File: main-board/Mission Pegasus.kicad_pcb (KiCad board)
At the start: 2 copper layers, 90.2 x 95.9 mm, 35 parts, among them J1 TC2030, M1 MountingHole, M2 MountingHole, M3 MountingHole, M4 MountingHole, Q1 DTC113Z, U2 4MB Flash, U3 AS72652, U4 AS72653, U6 AS72651, U7 RASPBERRY_PI_ZERO_2_W

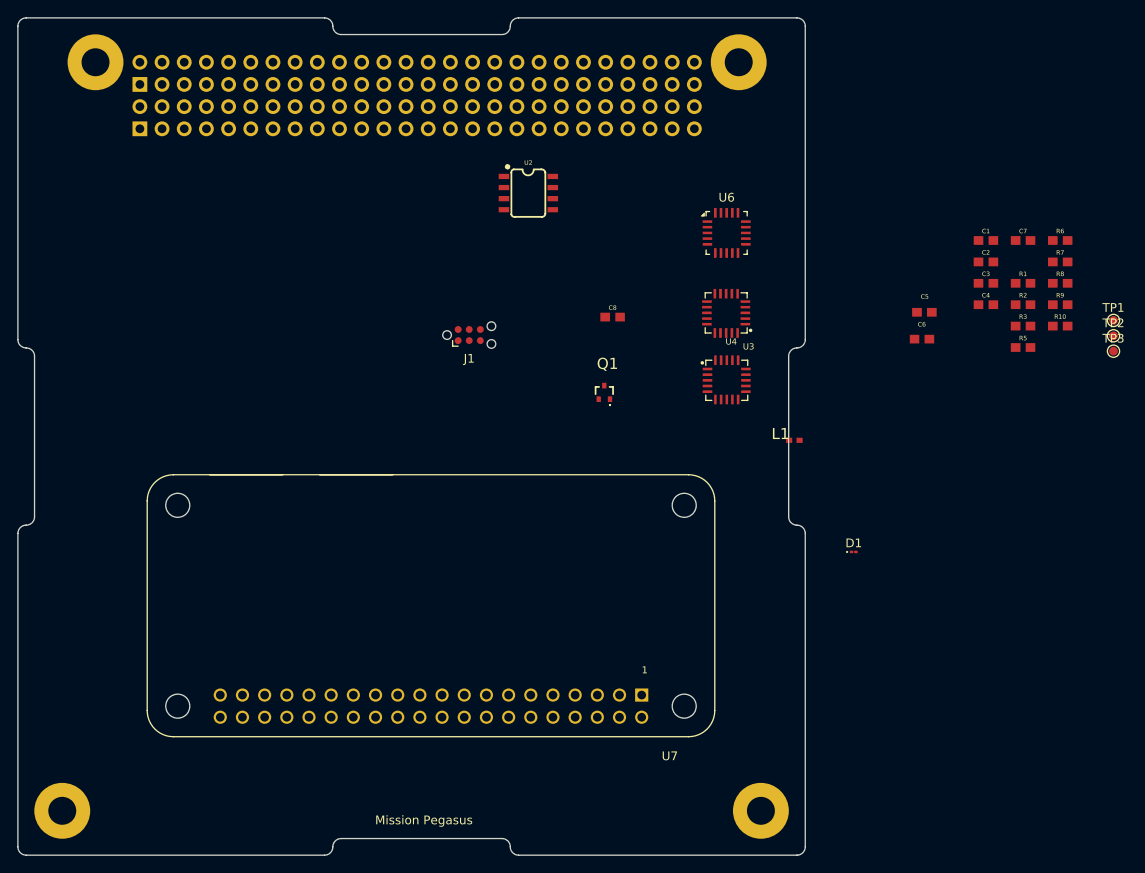
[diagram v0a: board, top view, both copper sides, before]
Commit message: Add Amphenol 20021311-00020T4LF (Minitek127) to mezzanine libraries
Import the Library Loader part (20-pin 1.27mm board-to-board connector)
into the mezzanine's SamacSys_Parts library: footprint, 3D model, and
symbol appended. 3D path rewritten to ${KIPRJMOD}-relative and the
symbol's Footprint property qualified with the library nickname.
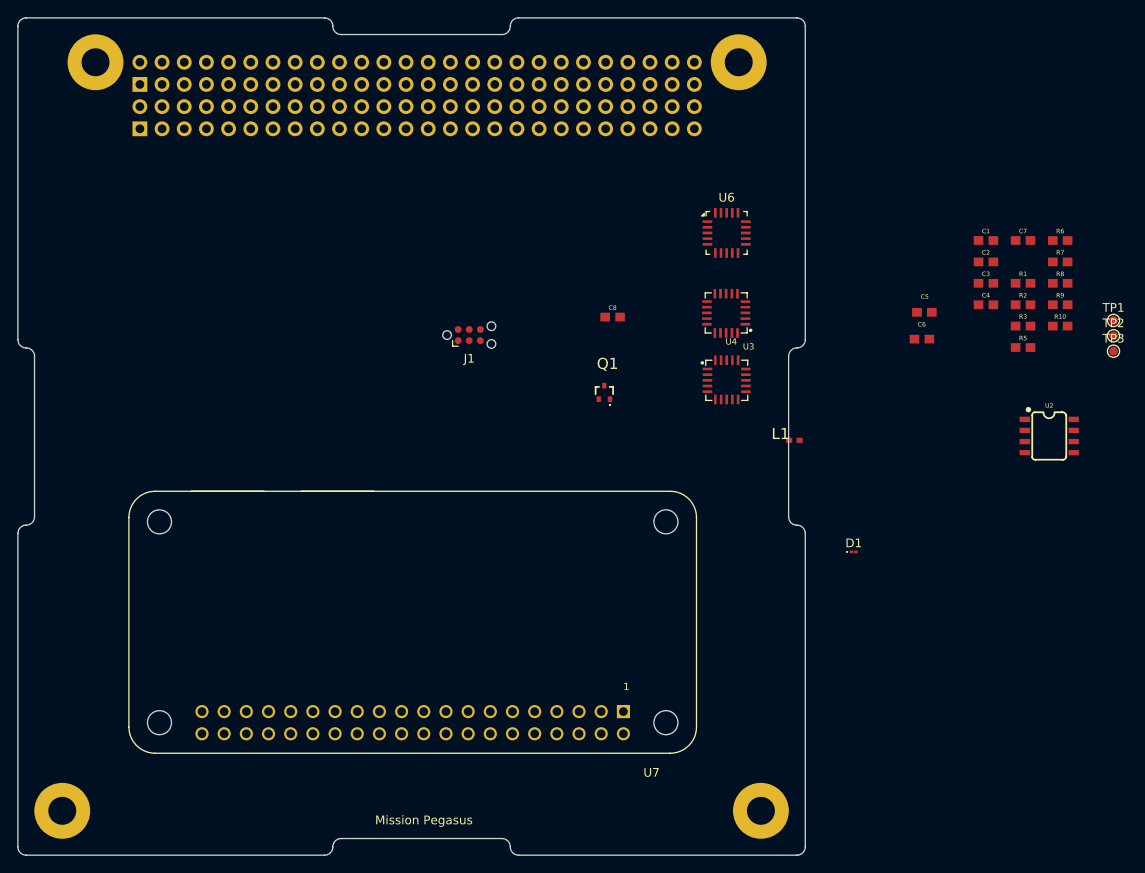
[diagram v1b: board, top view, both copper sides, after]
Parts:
- moved U2 65.8 mm to (209.1, 93.5)
- moved U7 2.82 mm to (136.2, 126.3)
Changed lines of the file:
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@@
 	(footprint "RPIZERO:RASPBERRYPI-ZERO_RPI-ZERO"
 		(layer "F.Cu")
-		(at 138.3075 124.4337 180)
+		(at 136.212 126.326 180)
 		(descr "Raspberry Pi board model B+, full outline with position of big connectors &amp; drill holes")
 		(property "Reference" "U7"
@@
 	(footprint "SparkfunLibrary:4MbFlash"
 		(layer "F.Cu")
-		(at 149.4581 65.681 -90)
+		(at 209.11 93.494 -90)
 		(descr "SOIC, 0.15 inch width")
 		(property "Reference" "U2"

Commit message: Attach Raspberry Pi Zero 2 W 3D model to RPi footprint
Add the mechanical STEP model of the Raspberry Pi Zero 2 W board
(RaspberryPi_Zero_2W.step, from the downloaded SolidWorks CAD) to
main-board 3dmodels, and reference it from the RASPBERRYPI-ZERO_RPI-ZERO
footprint via a ${KIPRJMOD}-relative path. Offset/rotation set to zero as
a starting point - needs alignment tuning in KiCad's 3D tab.
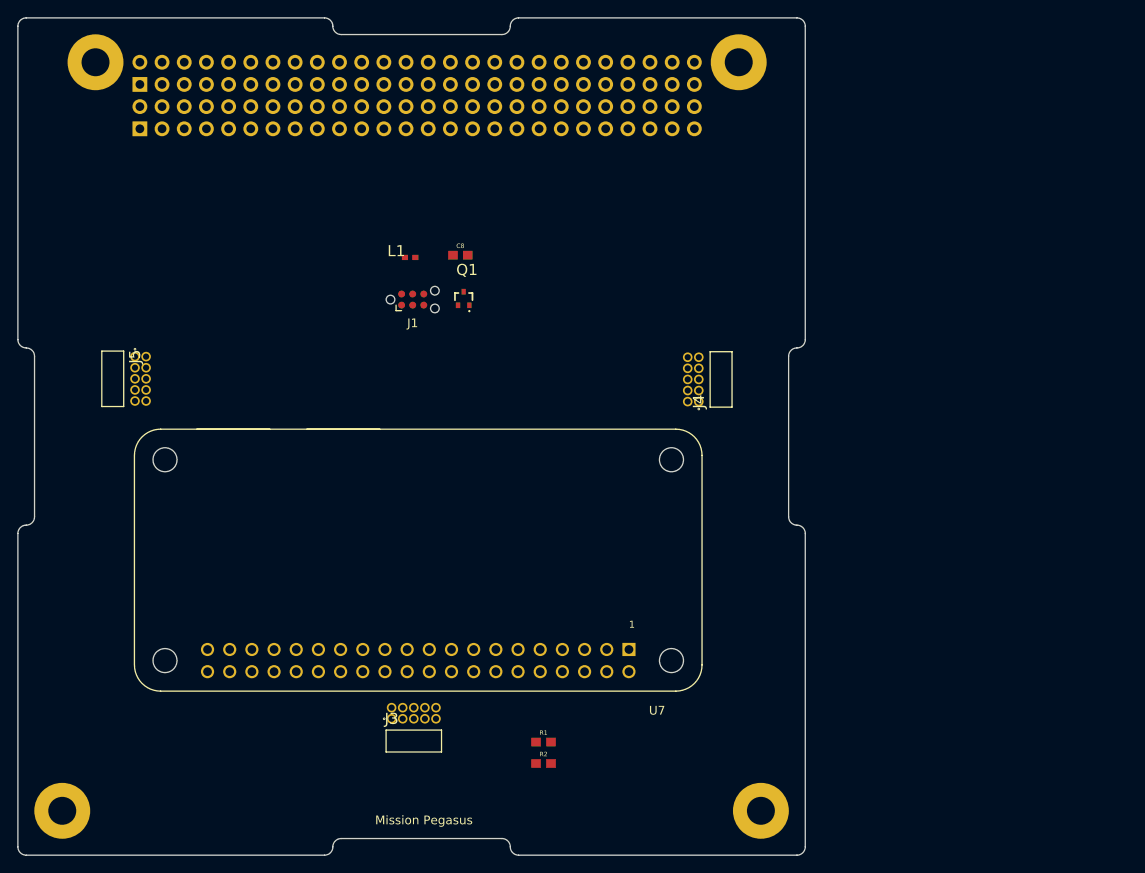
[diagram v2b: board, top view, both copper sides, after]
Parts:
- removed C1, C3, C5: 100nF, SparkfunLibrary:0603
- removed C2, C4, C6: 1 uF, SparkfunLibrary:0603
- removed C7: 1uF, SparkfunLibrary:0603
- removed D1: GREEN, LED_SMD:LED_01005_0402Metric
- removed R10, R9: 2k2, SparkfunLibrary:0603
- removed R3, R6, R7, R8: 10k, SparkfunLibrary:0603
- removed R5: 0R, SparkfunLibrary:0603
- removed TP1, TP2, TP3: TestPoint, TestPoint:TestPoint_Pad_D1.0mm
- removed U2: 4MB Flash, SparkfunLibrary:4MbFlash
- removed U3: AS72652, SparkfunLibrary:AS72651
- removed U4: AS72653, SparkfunLibrary:AS72651
- removed U6: AS72651, Package_LGA:AMS_LGA-20_4.7x4.5mm_P0.65mm
- added J3: FTSH-105-04-L-D-RA, SamacSys_Parts:FTSH-105-XX-YYY-D-RA, F.Cu at (133.8, 125.9)
- added J4: FTSH-105-04-L-D-RA, SamacSys_Parts:FTSH-105-XX-YYY-D-RA, F.Cu at (169.0, 89.6)
- added J5: FTSH-105-04-L-D-RA, SamacSys_Parts:FTSH-105-XX-YYY-D-RA, F.Cu at (104.4, 84.4)
- moved R1 76.0 mm to (151.2, 128.5)
- moved R2 76.0 mm to (151.2, 131.0)
- moved L1 48.7 mm to (135.9, 73.0)
- moved Q1 19.4 mm to (142.1, 77.7)
- moved C8 18.8 mm to (141.7, 72.8)
- moved J1 7.65 mm to (136.2, 77.9)
- moved U7 7.14 mm to (136.8, 119.2)

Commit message: Add Vishay CRCW06032K20FKEA (2.2k 0603) to mezzanine libraries
Import the Library Loader part (2.2k ohm 0603 resistor) into the
mezzanine's SamacSys_Parts library: footprint, 3D model, and symbol
appended. 3D path rewritten to ${KIPRJMOD}-relative and the symbol's
Footprint property qualified with the library nickname.
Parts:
- added H3: MountingHole, Mounting_Wuerth:Mounting_Wuerth_WA-SMSI-M2.5_H0.5mm_9774005151, F.Cu at (156.7, 136.2)
- added H4: MountingHole, Mounting_Wuerth:Mounting_Wuerth_WA-SMSI-M2.5_H0.5mm_9774005151, F.Cu at (116.3, 136.2)
- added H5: MountingHole, Mounting_Wuerth:Mounting_Wuerth_WA-SMSI-M2.5_H0.5mm_9774005151, F.Cu at (176.7, 67.0)
- added H6: MountingHole, Mounting_Wuerth:Mounting_Wuerth_WA-SMSI-M2.5_H0.5mm_9774005151, F.Cu at (95.7, 66.8)
- added H7: MountingHole, Mounting_Wuerth:Mounting_Wuerth_WA-SMSI-M2.5_H0.5mm_9774005151, F.Cu at (176.9, 108.1)
- added H8: MountingHole, Mounting_Wuerth:Mounting_Wuerth_WA-SMSI-M2.5_H0.5mm_9774005151, F.Cu at (95.6, 107.2)
- moved R2 43.9 mm to (135.7, 90.0)
- moved R1 43.9 mm to (135.7, 87.5)

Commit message: Update larger board design
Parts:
- H3, H4, H5, H6, H7, H8: footprint Mounting_Wuerth:Mounting_Wuerth_WA-SMSI-M2.5_H0.5mm_9774005151 -> MountingHole:MountingHole_2.7mm_M2.5
- moved J4 63.7 mm to (109.6, 112.5), turned to -90 degrees
- moved J5 58.6 mm to (162.6, 77.1), turned to 90 degrees
- moved U7 36.2 mm to (136.0, 83.0), turned to 0 degrees
- moved R1 33.0 mm to (105.7, 73.8)
- moved R2 31.9 mm to (106.7, 76.7), turned to 180 degrees
- moved H8 16.9 mm to (94.6, 124.1)
- moved Q1 13.6 mm to (152.9, 69.6)
- moved J3 13.5 mm to (146.8, 122.3)
- moved H6 13.3 mm to (94.6, 80.1)
- moved C8 9.12 mm to (139.7, 63.9), turned to 180 degrees
- moved J1 8.99 mm to (139.3, 69.4)
- moved L1 8.24 mm to (139.7, 65.7)
- moved H4 2.19 mm to (114.4, 137.3)
- moved H3 2.08 mm to (158.4, 137.3)
- moved H5 1.69 mm to (177.6, 65.5)
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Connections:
- H1 pad 25: /Stack Interface/5V_PERM -> +5V
- H1 pad 26: /Stack Interface/5V_PERM -> +5V
- H1 pad 33: /Stack Interface/GND -> GND
- H1 pad 34: /Stack Interface/GND -> GND
- H2 pad 25: /Stack Interface/5V_PERM -> +5V
- H2 pad 26: /Stack Interface/5V_PERM -> +5V
- H2 pad 29: /Stack Interface/GND -> GND
- H2 pad 30: /Stack Interface/GND -> GND
- H2 pad 31: /Stack Interface/GND -> GND
- H2 pad 32: /Stack Interface/GND -> GND
- J3 pad 1: SPI_MOSI -> CSN_EE
- J3 pad 10: INT -> GND
- J3 pad 2: SPI_SCK -> RX/SCL
- J3 pad 4: RESN -> TX/SDA
- J3 pad 5: CSN_EE -> SPI_MOSI
- J3 pad 6: GND -> INT
- J3 pad 7: RX/SCL -> SPI_SCK
- J3 pad 9: TX/SDA -> RESN
- J4 pad 1: SPI_MOSI -> CSN_EE
- J4 pad 10: INT -> GND
- J4 pad 2: SPI_SCK -> RX/SCL
- J4 pad 4: RESN -> TX/SDA
- J4 pad 5: CSN_EE -> SPI_MOSI
- J4 pad 6: GND -> INT
- J4 pad 7: RX/SCL -> SPI_SCK
- J4 pad 9: TX/SDA -> RESN
- J5 pad 1: SPI_MOSI -> CSN_EE
- J5 pad 10: INT -> GND
- J5 pad 2: SPI_SCK -> RX/SCL
- J5 pad 4: RESN -> TX/SDA
- J5 pad 5: CSN_EE -> SPI_MOSI
- J5 pad 6: GND -> INT
- J5 pad 7: RX/SCL -> SPI_SCK
- J5 pad 9: TX/SDA -> RESN
- U7 pad 2: unconnected-(U7-5V_2-Pad2) -> +5V
- U7 pad 4: unconnected-(U7-5V_4-Pad4) -> +5V
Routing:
- net GND: track 0.00 -> 213.9 mm, vias 0 -> 3
- net SPI_MOSI: track 0.00 -> 186.2 mm, vias 0 -> 3
- net +3.3V: track 0.00 -> 180.3 mm, vias 0 -> 1
- net RX/SCL: track 0.00 -> 169.7 mm
- net SPI_SCK: track 0.00 -> 168.3 mm
- net RESN: track 0.00 -> 155.5 mm, vias 0 -> 3
- net SPI_MISO: track 0.00 -> 154.3 mm, vias 0 -> 3
- net TX/SDA: track 0.00 -> 147.8 mm, vias 0 -> 3
- net CSN_EE: track 0.00 -> 125.1 mm, vias 0 -> 1
- net INT: track 0.00 -> 114.6 mm, vias 0 -> 4
- net +5V: track 0.00 -> 44.4 mm
- net Net-(Q1-B): track 0.00 -> 17.1 mm
- net Net-(J1-Pad2): track 0.00 -> 3.52 mm
- net /Stack Interface/CHARGE: track 0.00 -> 2.54 mm
- net /Stack Interface/BATT: track 0.00 -> 2.54 mm
- added copper zone on B.Cu, net GND

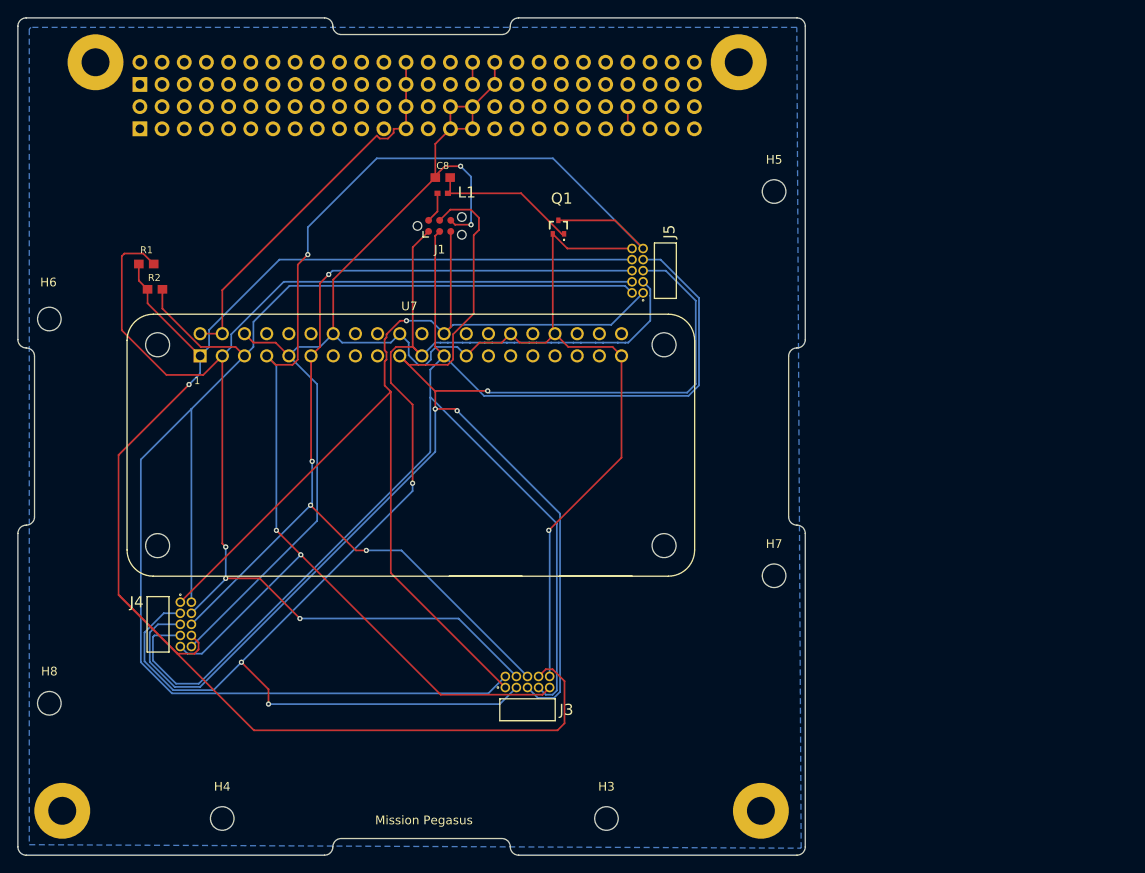
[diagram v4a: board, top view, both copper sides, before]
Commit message: Moved RA connectors back to 16mm away
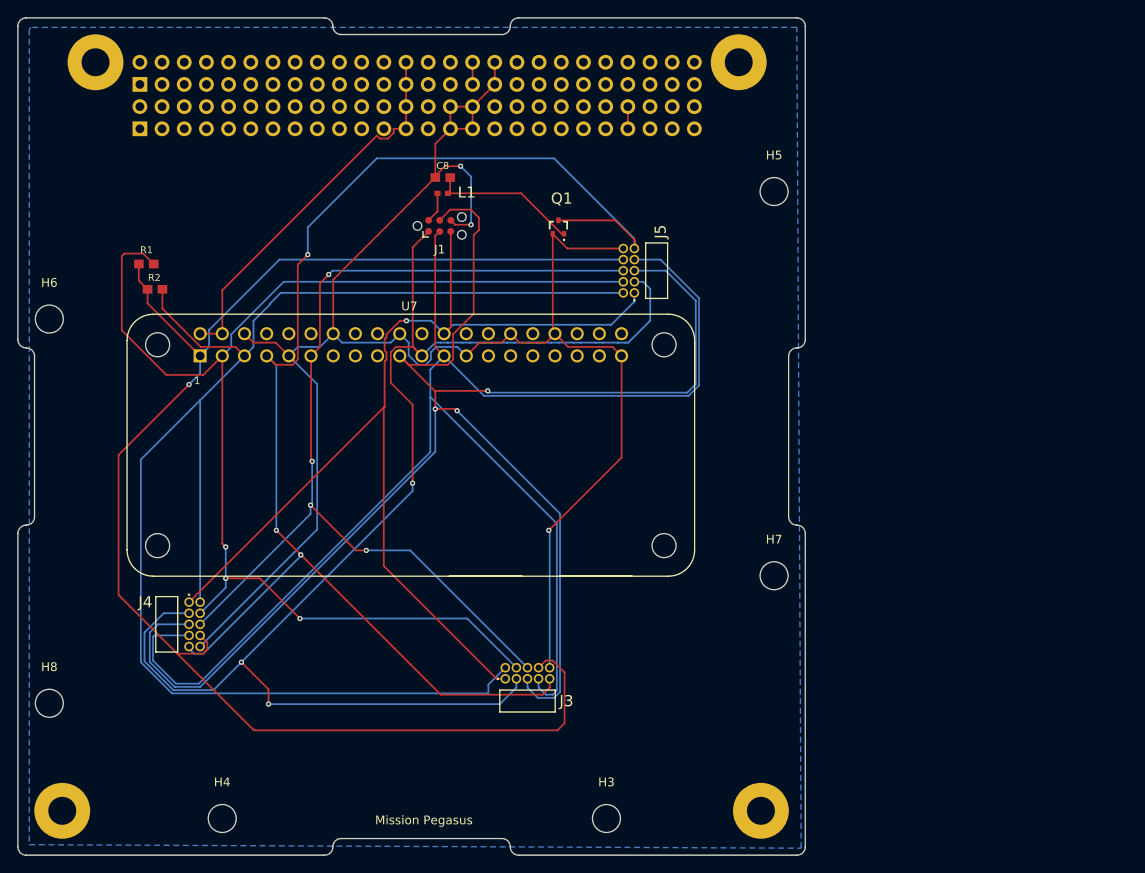
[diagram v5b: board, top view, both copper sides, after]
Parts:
- H3, H4, H5, H6, H7, H8: footprint MountingHole:MountingHole_2.7mm_M2.5 -> MountingHole:MountingHole_3.2mm_M3
- moved J3 1.00 mm to (146.8, 121.3)
- moved J4 1.00 mm to (110.6, 112.5)
- moved J5 1.00 mm to (161.6, 77.1)
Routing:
- net +3.3V: track 180.3 -> 171.9 mm
- net CSN_EE: track 125.1 -> 122.1 mm
- net SPI_SCK: track 168.3 -> 171.3 mm
- net SPI_MISO: track 154.3 -> 157.1 mm
- net SPI_MOSI: track 186.2 -> 189.0 mm
- net GND: track 213.9 -> 211.5 mm
- net TX/SDA: track 147.8 -> 146.0 mm
- net INT: track 114.6 -> 112.7 mm
